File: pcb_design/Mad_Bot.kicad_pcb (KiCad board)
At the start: 4 copper layers, 133.1 x 115.3 mm, 104 parts, among them IC1 RT6150BGQW, J1 EncoderConn, J2 EncoderConn, J3 EncoderConn, J4 LiPo, J5 TYPE-C-31-M-12, Q2 Q_PMOS_GSD, SW3 PWROFF_Switch, U1 MP6550GG-Z, U10 ArducamOV2640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

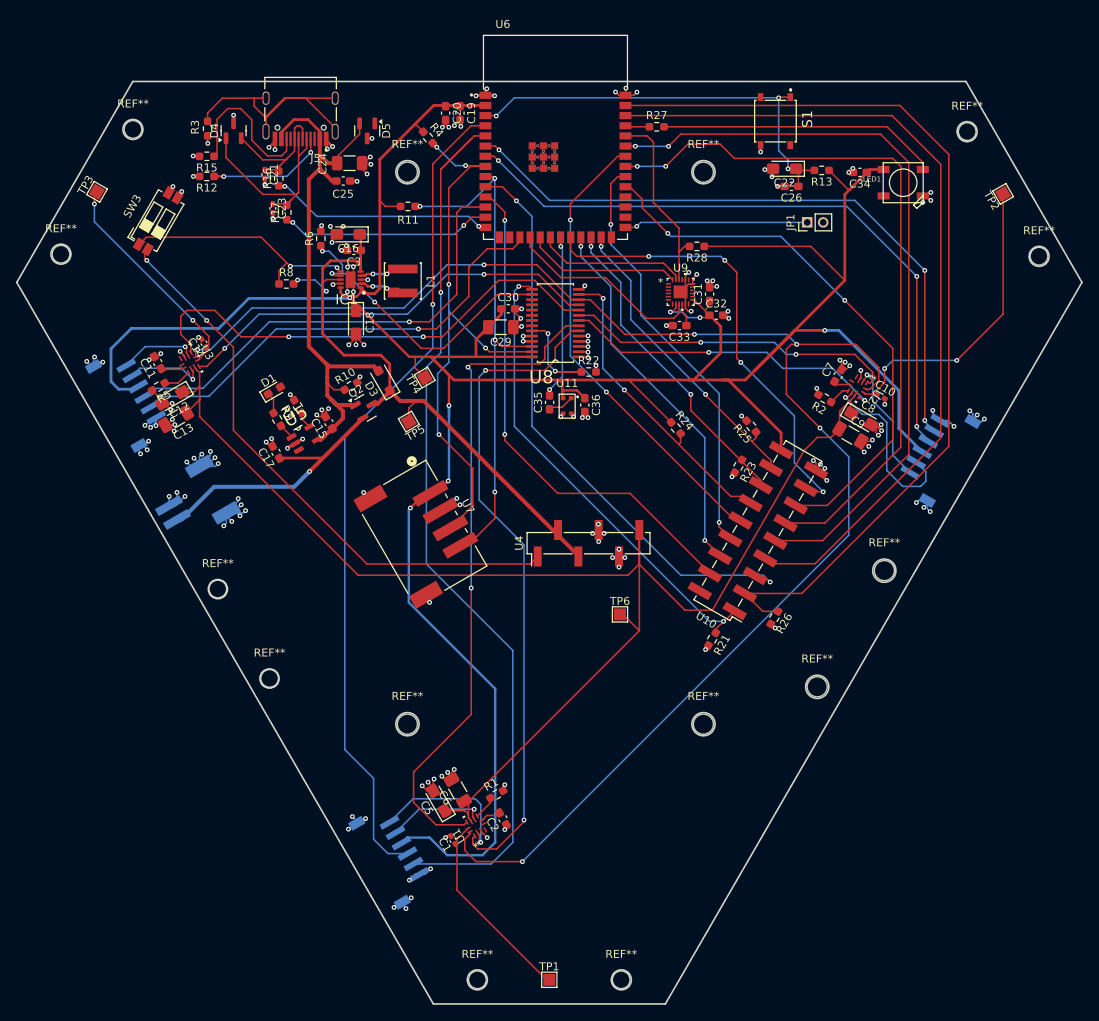
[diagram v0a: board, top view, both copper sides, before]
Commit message: Fixed silkscreen, modified PCB design, complied with DRC.
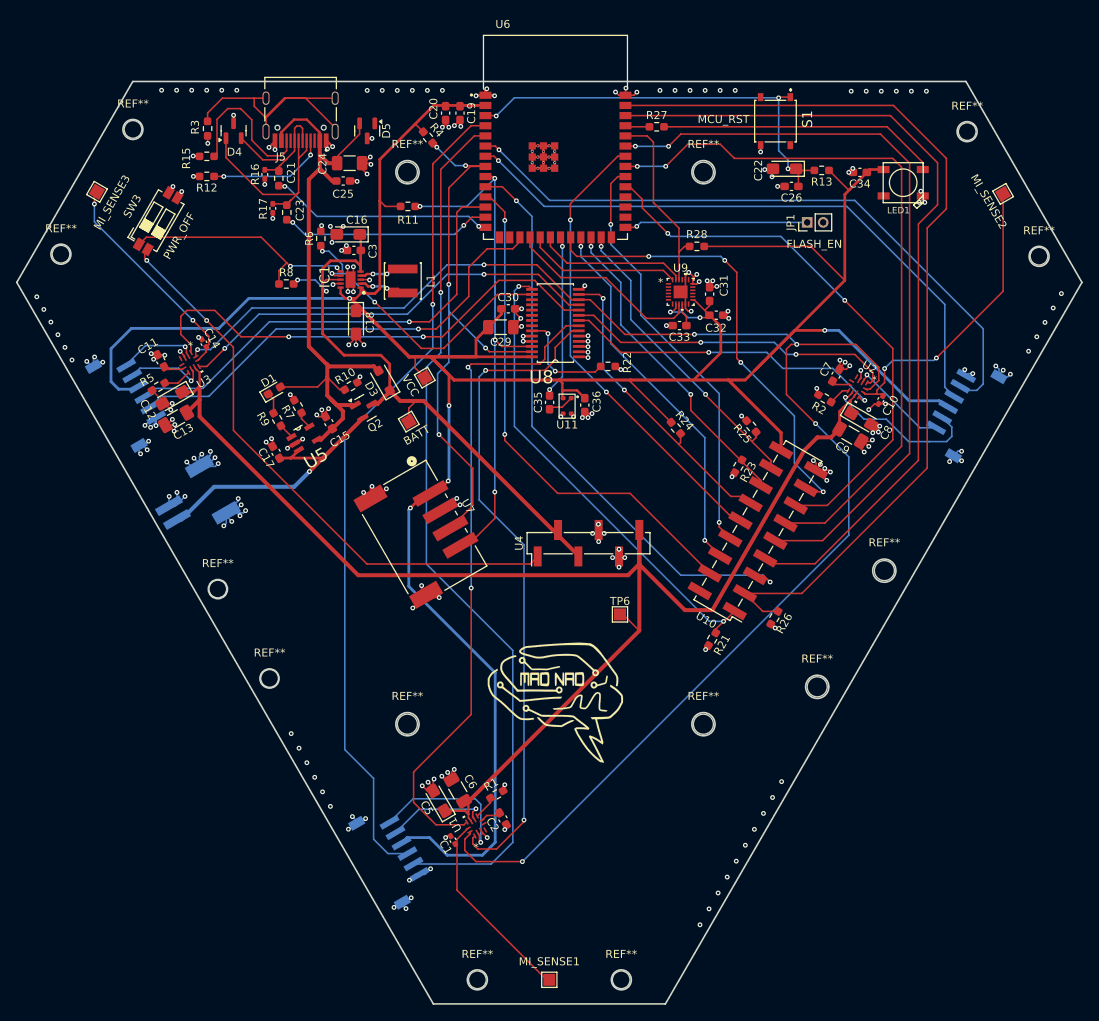
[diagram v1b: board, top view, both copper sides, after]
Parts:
- added G***: LOGO, NadSilk:brain_logo, F.Cu at (137.2, 117.3)
- moved J1 6.47 mm to (186.8, 79.9)
- moved R22 2.51 mm to (143.9, 75.5)
- moved C11 0.44 mm to (88.0, 74.8)
- moved C10 0.44 mm to (178.0, 79.7), turned to -120 degrees
- moved C7 0.26 mm to (172.4, 76.6)
- renumbered TP5 to BATT, TP1 to MI_SENSE1, TP2 to MI_SENSE2, TP3 to MI_SENSE3, TP4 to VCC
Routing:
- net GND: track 221.6 -> 249.0 mm, vias 176 -> 236
- net VBUS: track 73.5 -> 80.0 mm
- net ENC1_B: track 115.6 -> 110.2 mm
- net VCC: track 383.0 -> 378.3 mm
- net ENC2_A: track 81.5 -> 77.1 mm, vias 3 -> 1
- net M2_OUT1: track 15.5 -> 12.5 mm
- net M2_OUT2: track 22.5 -> 20.3 mm
- net Net-(Q2-S): track 41.1 -> 42.6 mm
- net Vdrive: track 160.5 -> 161.6 mm
- net CAM_PCLK: track 117.6 -> 116.9 mm
- net MI_SENSE2: track 38.0 -> 37.3 mm
- net ENC2_B: track 81.9 -> 82.0 mm, vias 3 -> 1
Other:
- board text added: "FLASH_EN"
- board text added: "MCU_RST"
- board text added: "PWR_OFF"

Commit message: Fixed mistake in battery bypass circuit.
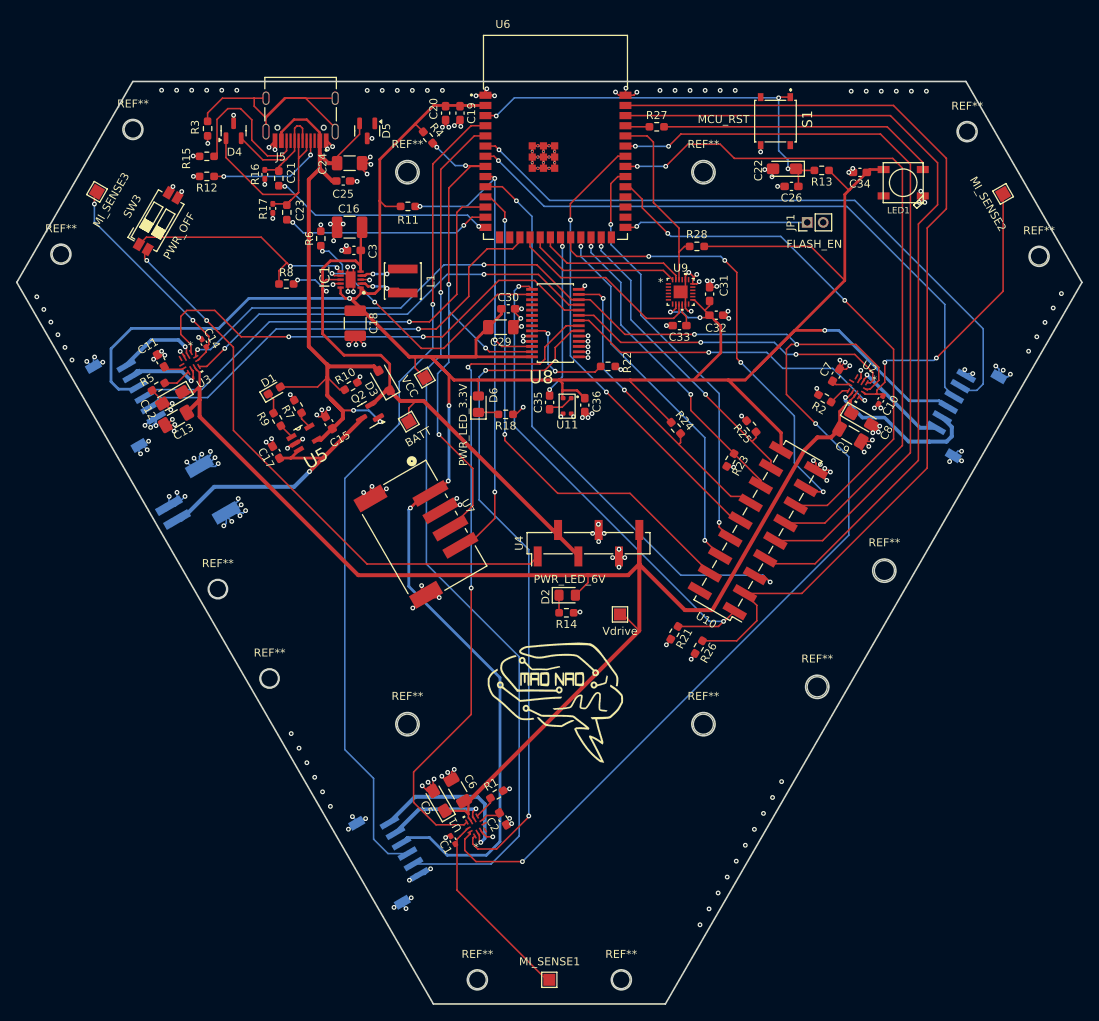
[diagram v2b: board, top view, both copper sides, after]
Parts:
- added D2: PWR_LED_6V, LED_SMD:LED_0805_2012Metric_Pad1.15x1.40mm_HandSolder, F.Cu at (138.8, 104.1)
- added D6: PWR_LED_3.3V, LED_SMD:LED_0805_2012Metric_Pad1.15x1.40mm_HandSolder, F.Cu at (127.7, 80.2)
- added R14: 1k, Resistor_SMD:R_0603_1608Metric_Pad0.98x0.95mm_HandSolder, F.Cu at (138.7, 106.3)
- added R18: 1k, Resistor_SMD:R_0603_1608Metric_Pad0.98x0.95mm_HandSolder, F.Cu at (131.1, 81.5)
- C16, C18: footprint Capacitor_Tantalum_SMD:CP_EIA-3216-18_Kemet-A_Pad1.58x1.35mm_HandSolder -> Capacitor_SMD:C_1210_3225Metric_Pad1.33x2.70mm_HandSolder
- R22: value 150k -> 250k
- moved R26 10.1 mm to (155.2, 110.6)
- moved R21 4.78 mm to (152.2, 108.8)
- moved R23 1.27 mm to (159.2, 87.2)
- moved Q2 0.92 mm to (113.9, 81.5), turned to -150 degrees
- moved C16 0.91 mm to (111.6, 58.1)
- moved C18 0.14 mm to (112.3, 70.1)
- renumbered MI_SENSE1 to TP1, MI_SENSE2 to TP2, MI_SENSE3 to TP3, VCC to TP4, BATT to TP5
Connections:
- C17 pad 1: Net-(Q2-S) -> Net-(Q2-D)
- J4 pad 2: Net-(Q2-S) -> Net-(Q2-D)
- Q2 pad 2: Net-(Q2-S) -> +BATT
- Q2 pad 3: +BATT -> Net-(Q2-D)
- U5 pad 3: Net-(Q2-S) -> Net-(Q2-D)
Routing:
- net Net-(Q2-S): track 42.6 -> 0.00 mm, vias 1 -> 0
- net Net-(Q2-D): track 0.00 -> 42.6 mm, vias 0 -> 1
- net CAM_PCLK: track 116.9 -> 123.7 mm
- net VBUS: track 80.0 -> 84.6 mm, vias 0 -> 2
- net CAM_PWDN: track 59.7 -> 63.8 mm
- net GND: track 249.0 -> 253.1 mm, vias 236 -> 239
- net Vdrive: track 161.6 -> 164.8 mm
- net VCC: track 378.3 -> 381.1 mm
- net Net-(D6-K): track 0.00 -> 2.60 mm
- net Net-(D2-K): track 0.00 -> 2.21 mm
- net M1_OUT1: track 19.0 -> 19.9 mm
- net ENC1_B: track 110.2 -> 110.9 mm
- net M3_OUT1: track 9.40 -> 9.98 mm
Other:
- board text added: "+"
- board text added: "-"

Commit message: Rerouted part of the board containing 3.3v regulator and USB connectivity. Routed 90ohm diff pair controlled-impedance traces for USB 2.0 Full Speed.
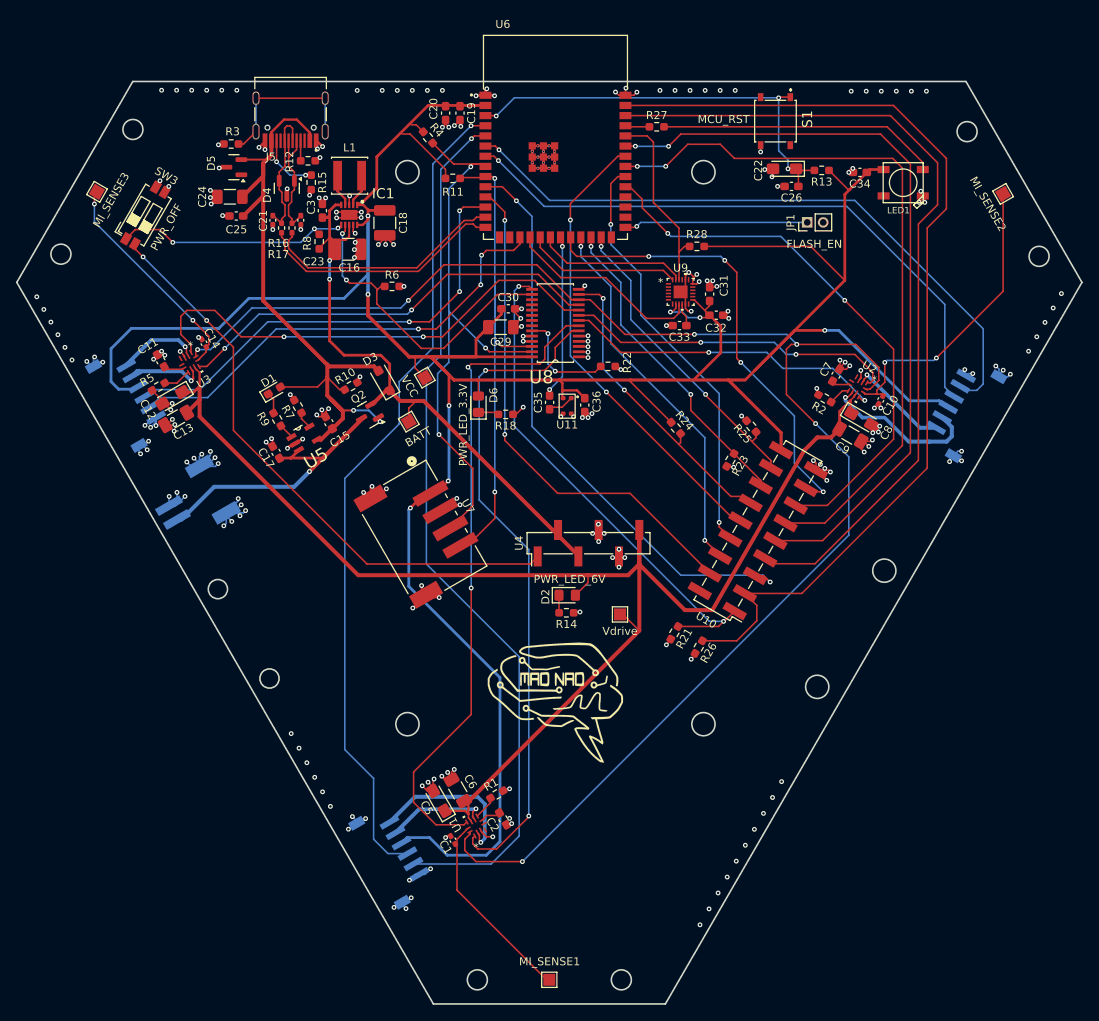
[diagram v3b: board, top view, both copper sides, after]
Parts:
- removed REF** (x8): MountingHole_2.2mm_M2, MountingHole:MountingHole_2.2mm_M2
- removed REF** (x6): MountingHole_2.5mm, MountingHole:MountingHole_2.5mm
- R16, R17: footprint Resistor_SMD:R_0603_1608Metric_Pad0.98x0.95mm_HandSolder -> Resistor_SMD:R_0402_1005Metric_Pad0.72x0.64mm_HandSolder
- moved D5 17.3 mm to (97.1, 50.6), turned to 180 degrees
- moved C24 15.5 mm to (96.6, 54.3), turned to 180 degrees
- moved L1 14.7 mm to (111.6, 51.7), turned to 0 degrees
- moved C25 14.1 mm to (97.4, 56.7), turned to 180 degrees
- moved R15 13.5 mm to (106.8, 52.5), turned to -90 degrees
- moved C18 13.1 mm to (116.0, 57.6)
- moved R12 12.8 mm to (106.4, 49.8), turned to 0 degrees
- moved R6 10.7 mm to (116.9, 65.5), turned to 0 degrees
- moved D4 9.80 mm to (103.8, 53.2), turned to -90 degrees
- moved IC1 8.09 mm to (111.5, 56.6), turned to -90 degrees
- moved R8 6.71 mm to (107.8, 59.9), turned to -90 degrees
- moved R11 6.61 mm to (124.5, 52.0)
- moved C3 6.33 mm to (108.2, 56.0), turned to 90 degrees
- moved R16 6.21 mm to (103.1, 58.2)
- moved C21 5.82 mm to (102.0, 57.2)
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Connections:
- net Net-(U6-IO19) renamed /MCU/N
- net Net-(U6-IO20) renamed /MCU/P
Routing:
- net Net-(J5-SHIELD-PadS1): track 35.3 -> 20.3 mm
- net USB_D-: track 28.5 -> 15.3 mm
- net Net-(J5-CC1): track 15.6 -> 2.74 mm, vias 2 -> 0
- net Net-(J5-CC2): track 19.7 -> 8.27 mm, vias 0 -> 2
- net VCC: track 381.1 -> 391.0 mm, vias 7 -> 8
- net I2C_SCL: track 73.2 -> 65.0 mm, vias 4 -> 3
- net +BATT: track 81.2 -> 76.4 mm
- net /MCU/N: track 26.3 -> 30.4 mm, vias 2 -> 0
- net VBUS: track 84.6 -> 88.3 mm
- net /MCU/P: track 28.2 -> 31.1 mm, vias 2 -> 0
- net GND: track 253.1 -> 251.3 mm
- net Net-(IC1-LX2): track 5.76 -> 4.08 mm, vias 2 -> 0
- net PWROFF_6V: track 72.2 -> 73.8 mm
- net Net-(IC1-LX1): track 5.62 -> 4.04 mm, vias 2 -> 0
- net USB_D+: track 18.1 -> 16.5 mm
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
